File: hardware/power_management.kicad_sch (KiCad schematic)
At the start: 5 parts, among them Q1 IRLML6402, U2 BMS Module

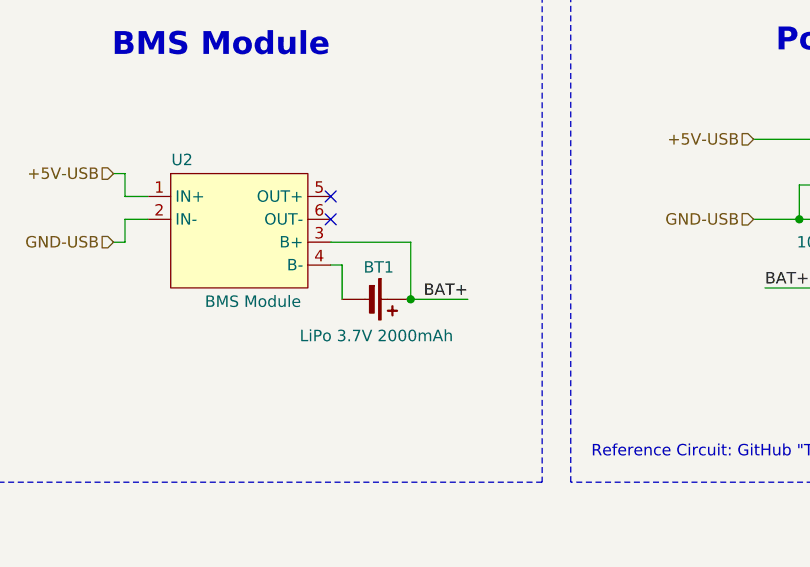
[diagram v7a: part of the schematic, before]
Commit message: Added the Power Switch and Test Points
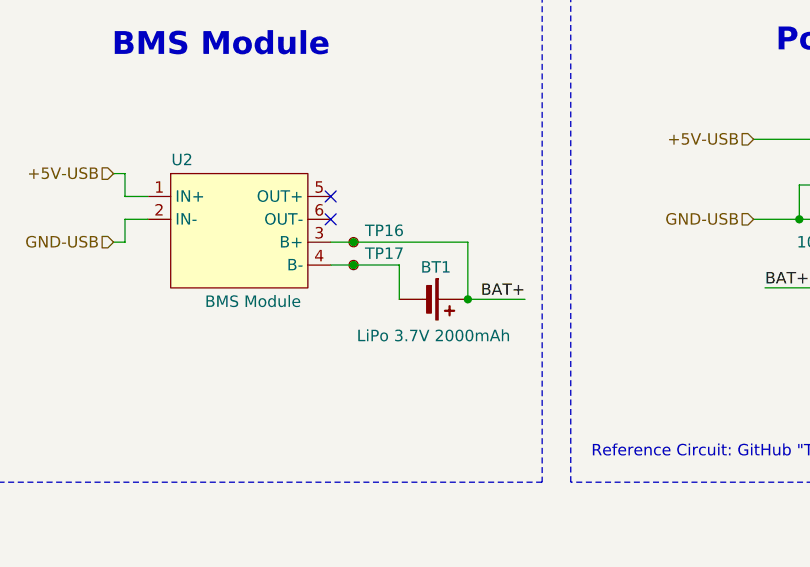
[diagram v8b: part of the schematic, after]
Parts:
- added TP16, TP17: TestPoint, symbol Connector:TestPoint_Small
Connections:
- net BAT+: now also TP16.1
- net at BT1.2 (-), U2.4 (B-): now also TP17.1
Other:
- moved on the sheet: BT1
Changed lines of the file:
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@@
+	)
+	(junction
+		(at 121.92 113.03)
+		(diameter 0)
+		(color 0 0 0 0)
+	)
+	(junction
+		(at 121.92 115.57)
+		(diameter 0)
+		(color 0 0 0 0)
 	)
 	(junction
@@
 	)
 	(junction
-		(at 128.27 119.38)
+		(at 134.62 119.38)
 		(diameter 0)
 		(color 0 0 0 0)
@@
 	(wire
 		(pts
-			(xy 120.65 115.57) (xy 120.65 119.38)
-		)
-		(stroke
-			(width 0)
-			(type default)
-		)
-	)
-	(wire
-		(pts
-			(xy 128.27 119.38) (xy 134.62 119.38)
+			(xy 127 115.57) (xy 127 119.38)
+		)
+		(stroke
+			(width 0)
+			(type default)
+		)
+	)
+	(wire
+		(pts
+			(xy 134.62 119.38) (xy 140.97 119.38)
 		)
 		(stroke
@@
 	(wire
 		(pts
-			(xy 128.27 113.03) (xy 128.27 119.38)
-		)
-		(stroke
-			(width 0)
-			(type default)
-		)
-	)
-	(wire
-		(pts
-			(xy 119.38 115.57) (xy 120.65 115.57)
+			(xy 121.92 113.03) (xy 134.62 113.03)
+		)
+		(stroke
+			(width 0)
+			(type default)
+		)
+	)
+	(wire
+		(pts
+			(xy 134.62 113.03) (xy 134.62 119.38)
+		)
+		(stroke
+			(width 0)
+			(type default)
+		)
+	)
+	(wire
+		(pts
+			(xy 119.38 115.57) (xy 121.92 115.57)
 		)
 		(stroke
@@
 	(wire
 		(pts
-			(xy 119.38 113.03) (xy 128.27 113.03)
+			(xy 119.38 113.03) (xy 121.92 113.03)
 		)
 		(stroke
@@
 		(pts
 			(xy 185.42 106.68) (xy 171.45 106.68)
+		)
+		(stroke
+			(width 0)
+			(type default)
+		)
+	)
+	(wire
+		(pts
+			(xy 121.92 115.57) (xy 127 115.57)
 		)
 		(stroke
@@
 	)
 	(label "BAT+"
-		(at 134.62 119.38 180)
+		(at 140.97 119.38 180)
 		(effects
 			(font
@@
 	)
 	(symbol
+		(lib_id "Connector:TestPoint_Small")
+		(at 121.92 113.03 0)
+		(unit 1)
+		(exclude_from_sim no)
+		(in_bom yes)
+		(on_board yes)
+		(dnp no)
+		(property "Reference" "TP16"
+			(at 123.19 111.7599 0)
+			(effects
+				(font
+					(size 1.27 1.27)
+				)
+				(justify left)
+			)
+		)
+		(property "Value" "TestPoint"
+			(at 121.666 109.474 0)
+			(effects
+				(font
+					(size 1.27 1.27)
+				)
+				(justify left)
+				(hide yes)
+			)
+		)
+		(property "Footprint" ""
+			(at 127 113.03 0)
+			(effects
+				(font
+					(size 1.27 1.27)
+				)
+				(hide yes)
+			)
+		)
+		(property "Datasheet" "~"
+			(at 127 113.03 0)
+			(effects
+				(font
+					(size 1.27 1.27)
+				)
+				(hide yes)
+			)
+		)
+		(property "Description" "test point"
+			(at 121.92 113.03 0)
+			(effects
+				(font
+					(size 1.27 1.27)
+				)
+				(hide yes)
+			)
+		)
+		(pin "1"
+		)
+		(instances
+			(project "kitchen_timer-hardware"
+				(path "/8963deea-96bc-4401-b671-98fbe9ed9c6a/c0498d1d-9e32-48f1-b749-4feb6881e262"
+					(reference "TP16")
+					(unit 1)
+				)
+			)
+		)
+	)
+	(symbol
 		(lib_id "Device:Battery_Cell")
-		(at 123.19 119.38 270)
+		(at 129.54 119.38 270)
 		(unit 1)
 		(exclude_from_sim no)
@@
 		(dnp no)
 		(property "Reference" "BT1"
-			(at 124.714 115.824 90)
+			(at 131.064 115.824 90)
 			(effects
 				(font
@@
 		)
 		(property "Value" "LiPo 3.7V 2000mAh"
-			(at 124.46 123.444 90)
+			(at 130.81 123.444 90)
 			(effects
 				(font
@@
 		)
 		(property "Footprint" ""
-			(at 124.714 119.38 90)
+			(at 131.064 119.38 90)
 			(effects
 				(font
@@
 		)
 		(property "Datasheet" "~"
-			(at 124.714 119.38 90)
+			(at 131.064 119.38 90)
 			(effects
 				(font
@@
 		)
 		(property "Description" "Single-cell battery"
-			(at 123.19 119.38 0)
+			(at 129.54 119.38 0)
 			(effects
 				(font
@@
 		)
 		(property "Supplier Link" ""
-			(at 123.19 119.38 0)
+			(at 129.54 119.38 0)
 			(effects
 				(font
@@
 		)
 		(property "Price/unit" ""
-			(at 123.19 119.38 0)
+			(at 129.54 119.38 0)
 			(effects
 				(font
@@
 		)
 		(property "Part Num" ""
-			(at 123.19 119.38 0)
+			(at 129.54 119.38 0)
 			(effects
 				(font
@@
 		)
 		(property "Package" ""
-			(at 123.19 119.38 0)
+			(at 129.54 119.38 0)
 			(effects
 				(font
@@
 					(unit 1)
 				)
+			)
+		)
+	)
+	(symbol
+		(lib_id "Connector:TestPoint_Small")
+		(at 121.92 115.57 0)
+		(unit 1)
+		(exclude_from_sim no)
+		(in_bom yes)
+		(on_board yes)
+		(dnp no)
+		(property "Reference" "TP17"
+			(at 123.19 114.2999 0)
+			(effects
+				(font
+					(size 1.27 1.27)
+				)
+				(justify left)
+			)
+		)
+		(property "Value" "TestPoint"
+			(at 121.666 112.014 0)
+			(effects
+				(font
+					(size 1.27 1.27)
+				)
+				(justify left)
+				(hide yes)
+			)
+		)
+		(property "Footprint" ""
+			(at 127 115.57 0)
+			(effects
+				(font
+					(size 1.27 1.27)
+				)
+				(hide yes)
+			)
+		)
+		(property "Datasheet" "~"
+			(at 127 115.57 0)
+			(effects
+				(font
+					(size 1.27 1.27)
+				)
+				(hide yes)
+			)
+		)
+		(property "Description" "test point"
+			(at 121.92 115.57 0)
+			(effects
+				(font
+					(size 1.27 1.27)
+				)
+				(hide yes)
+			)
+		)
+		(pin "1"
+		)
+		(instances
+			(project "kitchen_timer-hardware"
+				(path "/8963deea-96bc-4401-b671-98fbe9ed9c6a/c0498d1d-9e32-48f1-b749-4feb6881e262"
+					(reference "TP17")
+					(unit 1)
+				)
